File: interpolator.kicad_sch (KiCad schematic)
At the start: 45 parts, among them J2 Conn_02x05_Top_Bottom, SW1 SW_RCLK, SW2 SW_SG1, SW3 SW_SG0, SW4 SW_ROT, SW5 SW_SF1, SW6 SW_SF0, U1 iC-NV

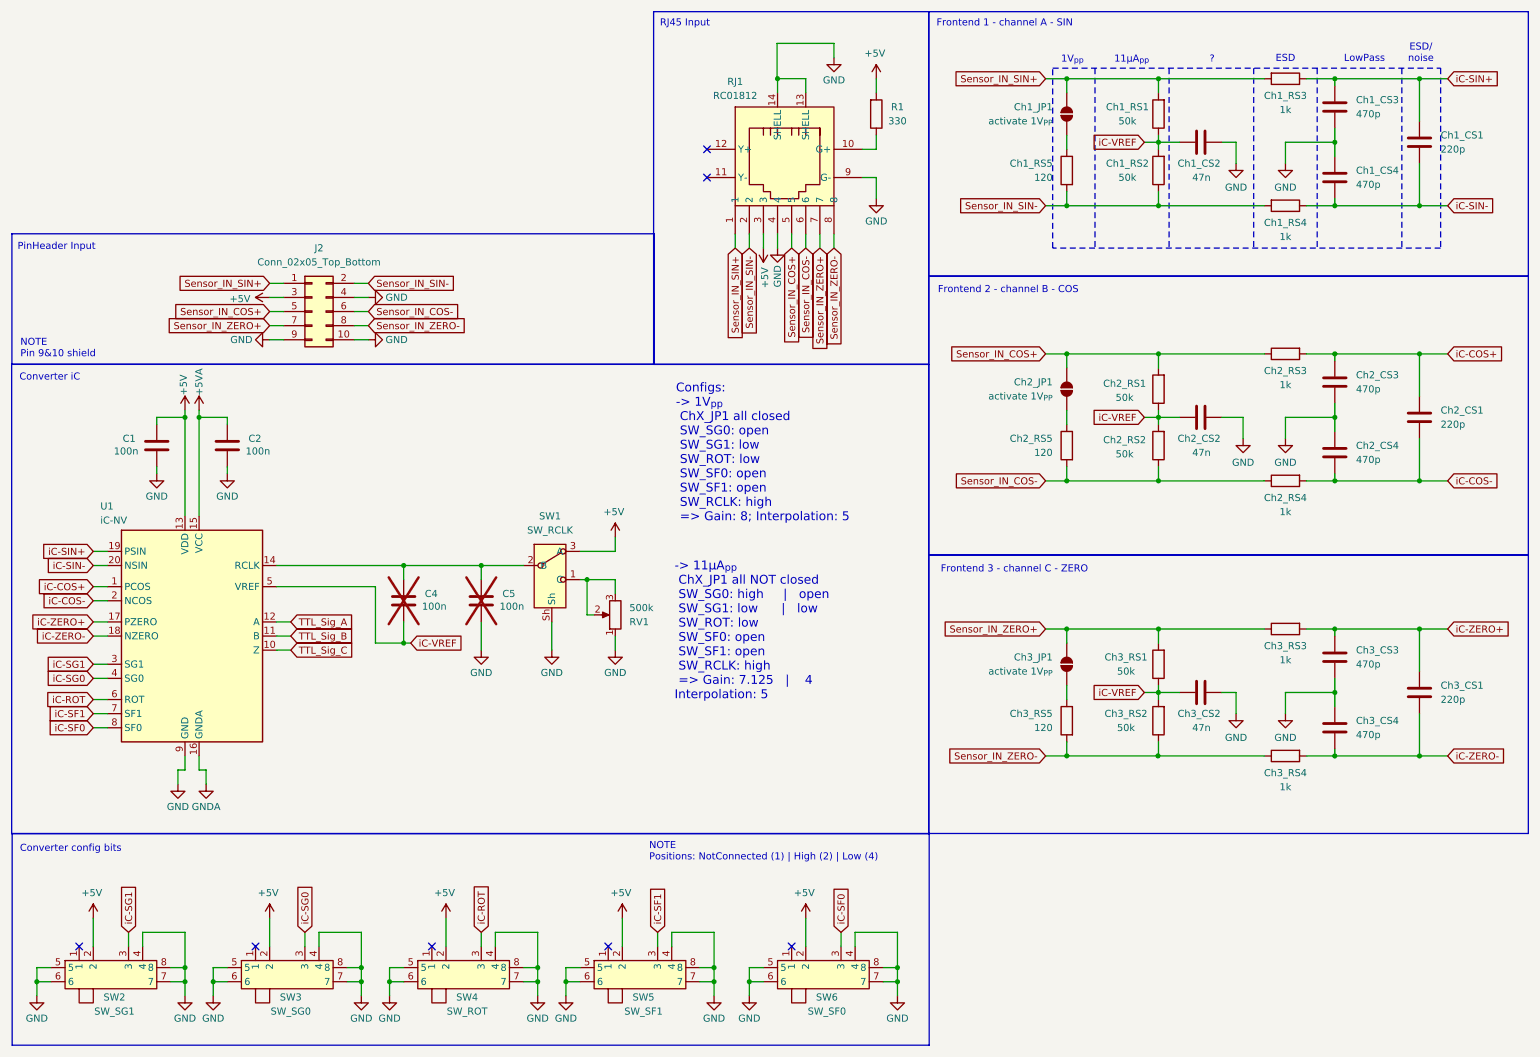
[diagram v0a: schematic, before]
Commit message: further ESD protection, PCB layout started
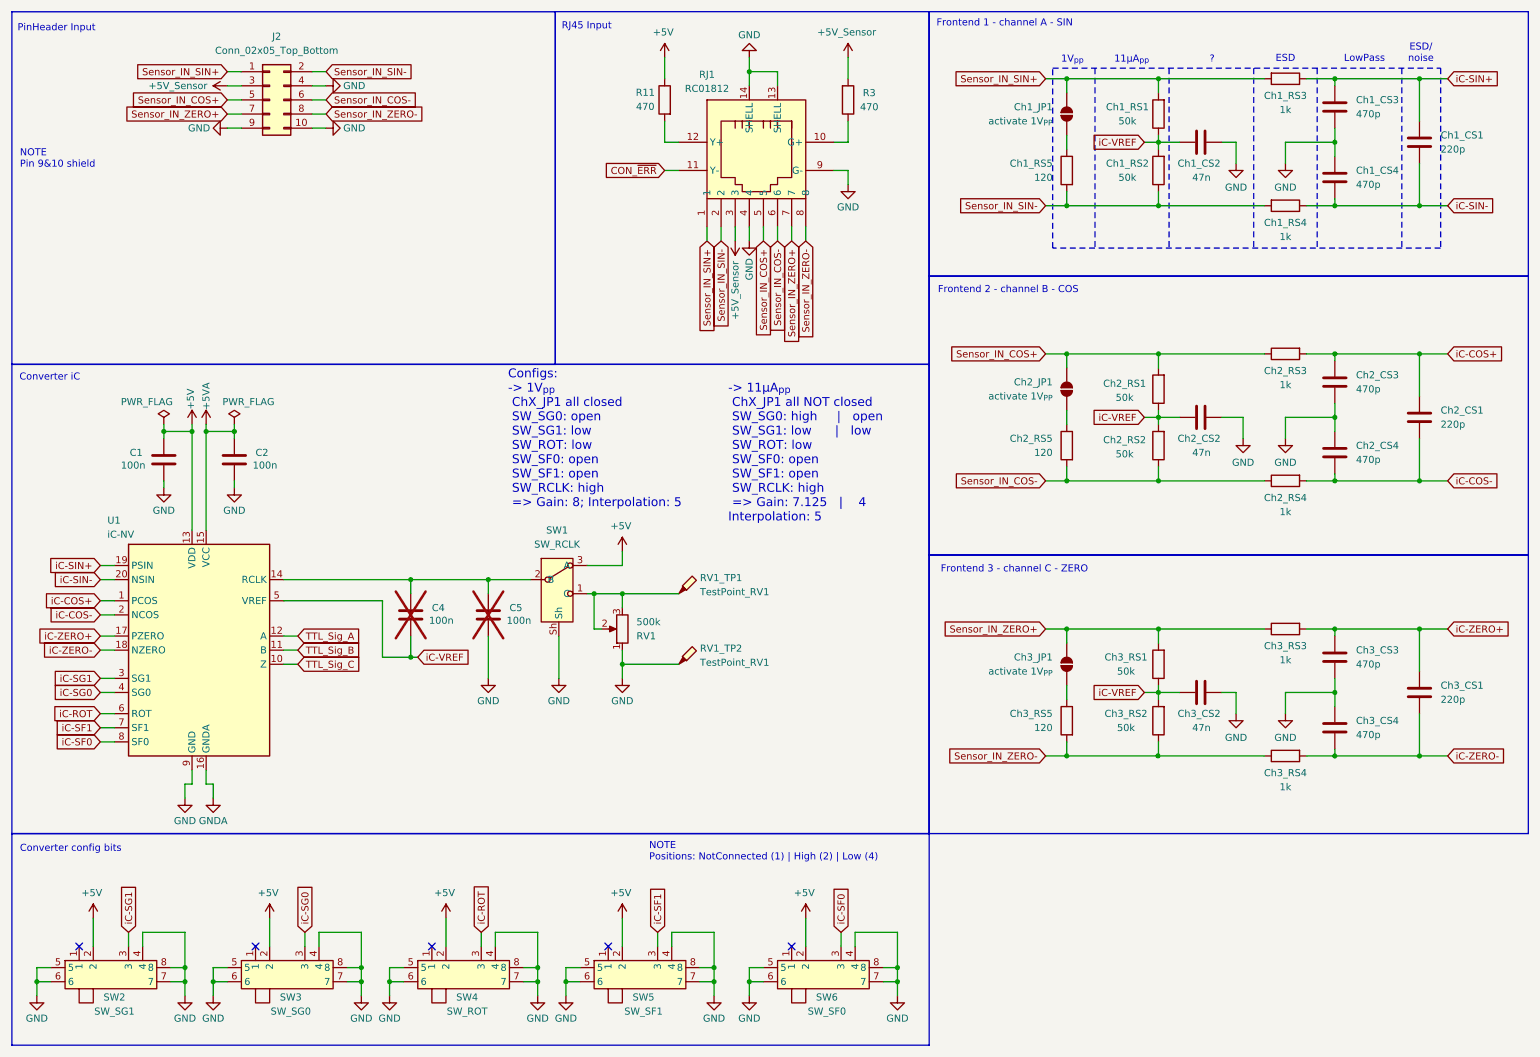
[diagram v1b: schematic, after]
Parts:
- added R11: 470, Resistor_SMD:R_0603_1608Metric, symbol Device:R
- added RV1_TP1: TestPoint_RV1, TestPoint:TestPoint_THTPad_2.0x2.0mm_Drill1.0mm, symbol Connector:TestPoint_Probe
- added RV1_TP2: TestPoint_RV1, TestPoint:TestPoint_THTPad_D2.0mm_Drill1.0mm, symbol Connector:TestPoint_Probe
- R3: renamed from R1; value 330 -> 470
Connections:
- net +5V: now also R11.1; no longer J2.3 (Pin_3), R3.2, RJ1.3
- net GND: now also RV1_TP2.1
- net CON_~{ERR}: now reaches RJ1.11 (Y-)
- net at RJ1.12 (Y+): now also R11.2
- net at RV1.2, RV1.3, SW1.1 (C): now also RV1_TP1.1
- new net +5V_Sensor: J2.3 (Pin_3), R3.2, RJ1.3
- no-connect marks 7 -> 5
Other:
- moved on the sheet: C1, C2, C4, C5, J2, R3, RJ1, RV1, SW1, U1

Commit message: first theoretical working PCB finished (v0.9.3)
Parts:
- added R4: 10k, Resistor_SMD:R_0603_1608Metric, symbol Device:R
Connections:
- net +5V: now also R4.1
- net CON_~{ERR}: now also R4.2
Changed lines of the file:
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@@
 	(wire
 		(pts
+			(xy 92.71 63.5) (xy 95.25 63.5)
+		)
+		(stroke
+			(width 0)
+			(type default)
+		)
+	)
+	(wire
+		(pts
 			(xy 106.68 189.23) (xy 106.68 186.69)
 		)
@@
 	(wire
 		(pts
+			(xy 95.25 58.42) (xy 95.25 63.5)
+		)
+		(stroke
+			(width 0)
+			(type default)
+		)
+	)
+	(wire
+		(pts
 			(xy 265.43 24.13) (xy 265.43 31.75)
 		)
@@
 	(wire
 		(pts
+			(xy 95.25 50.8) (xy 95.25 46.99)
+		)
+		(stroke
+			(width 0)
+			(type default)
+		)
+	)
+	(wire
+		(pts
 			(xy 245.11 73.66) (xy 250.19 73.66)
 		)
@@
 		)
 	)
+	(global_label "CON_~{ERR}"
+		(shape input)
+		(at 92.71 63.5 180)
+		(fields_autoplaced yes)
+		(effects
+			(font
+				(size 1.27 1.27)
+			)
+			(justify right)
+		)
+		(property "Intersheetrefs" "${INTERSHEET_REFS}"
+			(at 81.1372 63.5 0)
+			(effects
+				(font
+					(size 1.27 1.27)
+				)
+				(justify right)
+				(hide yes)
+			)
+		)
+	)
 	(global_label "Sensor_IN_ZERO-"
 		(shape input)
@@
 	)
 	(symbol
+		(lib_id "Device:R")
+		(at 95.25 54.61 0)
+		(mirror y)
+		(unit 1)
+		(exclude_from_sim no)
+		(in_bom yes)
+		(on_board yes)
+		(dnp no)
+		(property "Reference" "R4"
+			(at 91.7575 53.2765 0)
+			(effects
+				(font
+					(size 1.27 1.27)
+				)
+			)
+		)
+		(property "Value" "10k"
+			(at 91.7575 55.8165 0)
+			(effects
+				(font
+					(size 1.27 1.27)
+				)
+			)
+		)
+		(property "Footprint" "Resistor_SMD:R_0603_1608Metric"
+			(at 97.028 54.61 90)
+			(effects
+				(font
+					(size 1.27 1.27)
+				)
+				(hide yes)
+			)
+		)
+		(property "Datasheet" "~"
+			(at 95.25 54.61 0)
+			(effects
+				(font
+					(size 1.27 1.27)
+				)
+				(hide yes)
+			)
+		)
+		(property "Description" "Resistor"
+			(at 95.25 54.61 0)
+			(effects
+				(font
+					(size 1.27 1.27)
+				)
+				(hide yes)
+			)
+		)
+		(pin "2"
+		)
+		(pin "1"
+		)
+		(instances
+			(project "SinCosEnc-Converter_EP5101-0011"
+				(path "/65c0920c-b33d-485e-a4e4-15145e9bcf4b/3a1cba1a-78b8-4283-a679-1de86586ecf3"
+					(reference "R4")
+					(unit 1)
+				)
+			)
+		)
+	)
+	(symbol
 		(lib_id "power:GND")
 		(at 232.41 138.43 0)
@@
 					(unit 1)
 				)
+			)
+		)
+	)
+	(symbol
+		(lib_id "power:+5V")
+		(at 95.25 46.99 0)
+		(unit 1)
+		(exclude_from_sim no)
+		(in_bom yes)
+		(on_board yes)
+		(dnp no)
+		(property "Reference" "#PWR069"
+			(at 95.25 50.8 0)
+			(effects
+				(font
+					(size 1.27 1.27)
+				)
+				(hide yes)
+			)
+		)
+		(property "Value" "+5V"
+			(at 94.996 42.418 0)
+			(effects
+				(font
+					(size 1.27 1.27)
+				)
+			)
+		)
+		(property "Footprint" ""
+			(at 95.25 46.99 0)
+			(effects
+				(font
+					(size 1.27 1.27)
+				)
+				(hide yes)
+			)
+		)
+		(property "Datasheet" ""
+			(at 95.25 46.99 0)
+			(effects
+				(font
+					(size 1.27 1.27)
+				)
+				(hide yes)
+			)
+		)
+		(property "Description" "Power symbol creates a global label with name \"+5V\""
+			(at 95.25 46.99 0)
+			(effects
+				(font
+					(size 1.27 1.27)
+				)
+				(hide yes)
+			)
+		)
+		(pin "1"
+		)
+		(instances
+			(project "SinCosEnc-Converter_EP5101-0011"
+				(path "/65c0920c-b33d-485e-a4e4-15145e9bcf4b/3a1cba1a-78b8-4283-a679-1de86586ecf3"
+					(reference "#PWR069")
+					(unit 1)
+				)

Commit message: version 0.9.6 finished
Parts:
- removed J2: Conn_02x05_Top_Bottom, Connector_PinHeader_2.54mm:PinHeader_2x05_P2.54mm_Horizontal, symbol Connector_Generic:Conn_02x05_Odd_Even
- removed RJ1: RC01812, easyeda2kicad:RJ45-TH_RC01812, symbol easyeda2kicad:RC01812
- added D8: LED RED, LED_SMD:LED_0603_1608Metric, symbol Device:LED
- added D9: LED GREEN, LED_SMD:LED_0603_1608Metric, symbol Device:LED
- added J1: Conn_02x05_Top_Bottom, Connector_PinHeader_2.54mm:PinHeader_2x05_P2.54mm_Horizontal, symbol Connector_Generic:Conn_02x05_Odd_Even
- added RJ1: 6339160-1, easyeda2kicad:RJ45-SMD_6339160-1, symbol easyeda2kicad:6339160-1
- C4, C5: now fitted
- Ch1_RS1, Ch1_RS2, Ch2_RS1, Ch2_RS2, Ch3_RS1, Ch3_RS2: LCSC Part (none) -> C861451
- RV1: value 500k -> 50k; footprint Potentiometer_THT:Potentiometer_Bourns_3296P_Horizontal -> Potentiometer_THT:Potentiometer_Bourns_3266X_Horizontal; LCSC Part C780107 -> C780222
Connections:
- net +5VA is gone; now on net +5V: C2.2, U1.15 (VCC)
- net GNDA is gone; now on net GND: U1.16 (GNDA)
- net +5V_Sensor: now also J1.9 (Pin_9), RJ1.3
- net CON_~{ERR}: now also D8.1 (K)
- net GND: now also D9.1 (K), J1.7 (Pin_7), RJ1.6
- net Sensor_IN_COS+: now also J1.3 (Pin_3), RJ1.4
- net Sensor_IN_COS-: now also J1.4 (Pin_4), RJ1.5
- net Sensor_IN_SIN+: now also J1.1 (Pin_1), RJ1.1
- net Sensor_IN_SIN-: now also J1.2 (Pin_2), RJ1.2
- net Sensor_IN_ZERO+: now also J1.5 (Pin_5), RJ1.7
- net Sensor_IN_ZERO-: now also J1.6 (Pin_6), RJ1.8
- net at R11.2: now also D8.2 (A)
- net at R3.1: now also D9.2 (A)
- new net GNDS: J1.10 (Pin_10), J1.8 (Pin_8), RJ1.10, RJ1.9
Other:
- note added: "Configs: -> 1V_{pp} ChX_JP1 all closed SW_SG0: open SW_SG1: low SW_ROT: low SW_SF0: open SW_SF1: open SW_RCLK: high => Gain: 8 Interpolation: 5"
- note added: "ESD & LowPass"
- note added: "Status LEDs"
- note removed: "?"
- note removed: "Configs: -> 1V_{pp} ChX_JP1 all closed SW_SG0: open SW_SG1: low SW_ROT: low SW_SF0: open SW_SF1: open SW_RCLK: high => Gain: 8; Interpolation: 5"
- note removed: "ESD"
- note removed: "LowPass"
- note removed: "NOTE Pin 9&10 shield"
- moved on the sheet: R11, R3, R4
